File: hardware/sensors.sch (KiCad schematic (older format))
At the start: 43 parts, among them P13 CONN_01X02_MTMP, P14 CONN_01X02_BTMP, U1 LM358A, U2 LAH-100P, U3 LOC110, U4 MCP6001, U5 ADA4805-1

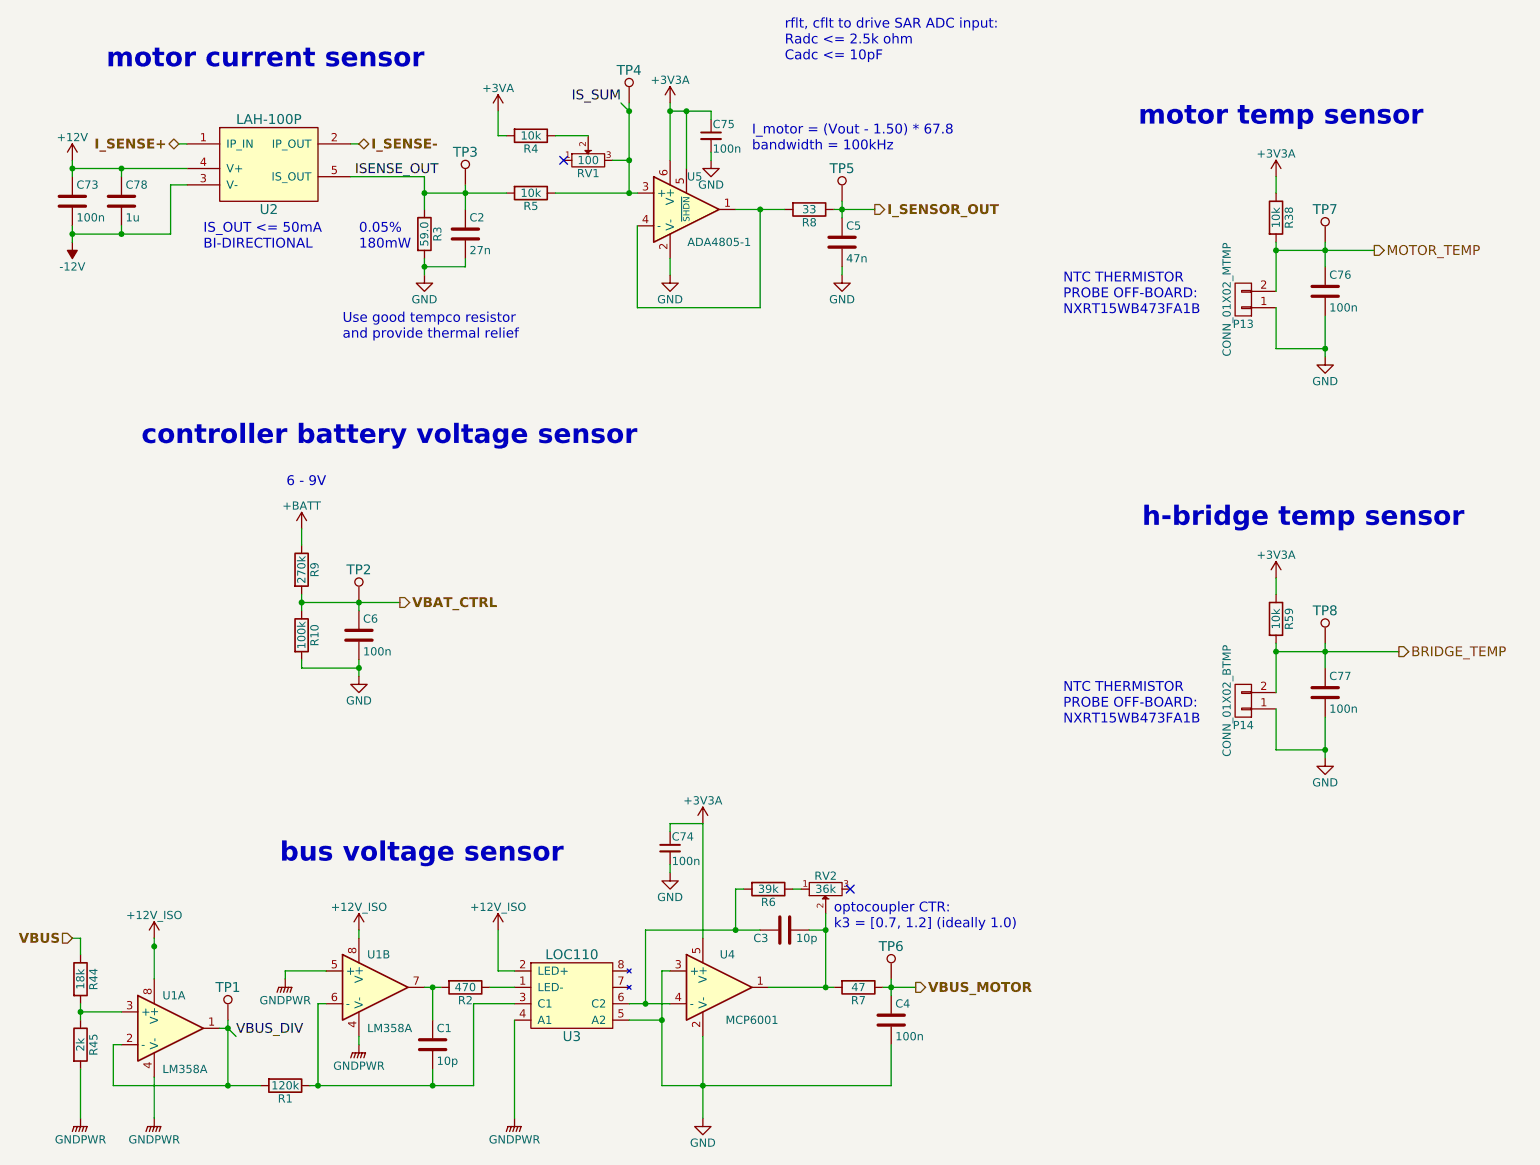
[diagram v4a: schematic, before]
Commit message: Create and verify full Digikey BOM
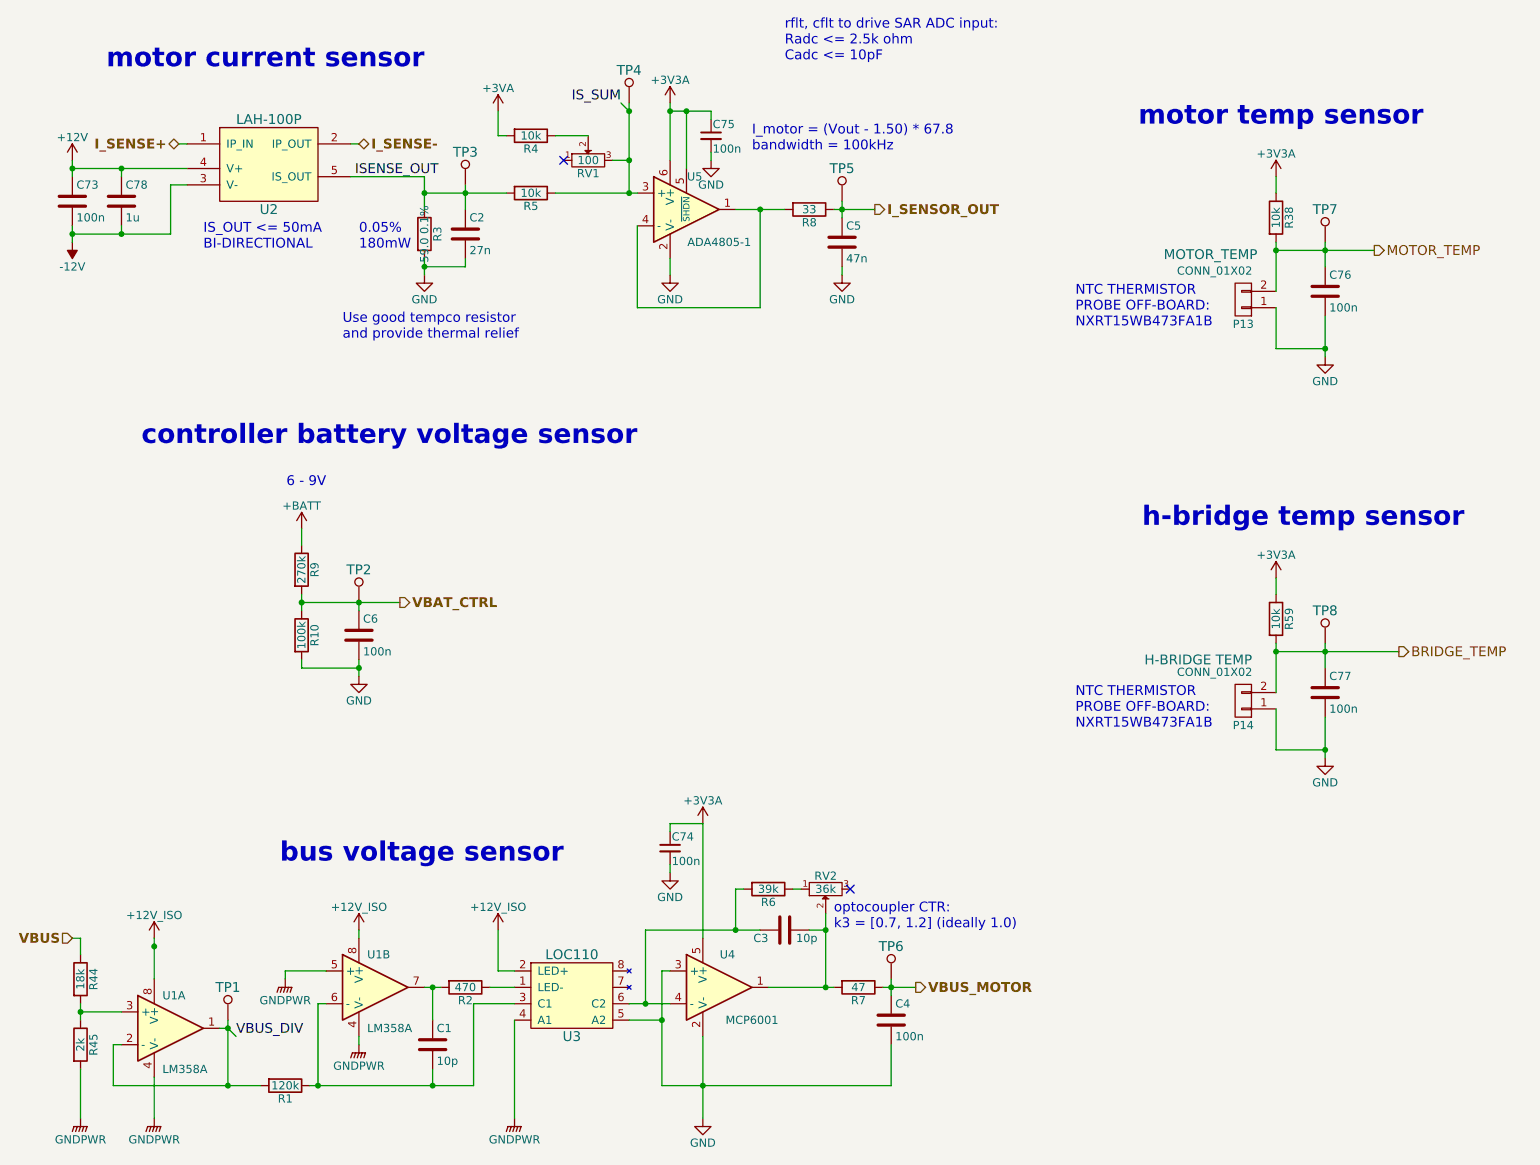
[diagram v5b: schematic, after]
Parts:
- C1, C2, C3, C4, C5, C6, C74, C75, C76, C77: Voltage (none) -> 16V
- C73, C78: Voltage (none) -> 25V
- P13: value CONN_01X02_MTMP -> CONN_01X02; Use (none) -> MOTOR_TEMP
- P14: value CONN_01X02_BTMP -> CONN_01X02; Use (none) -> H-BRIDGE TEMP
- R3: value 59.0 -> 59.0 0.1%
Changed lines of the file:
@@
 P 3100 2000
 F 0 "R3" V 3180 2000 50  0000 C CNN
-F 1 "59.0" V 3100 2000 50  0000 C CNN
+F 1 "59.0 0.1%" V 3100 2000 50  0000 C CNN
 F 2 "Resistors_SMD:R_1206" V 3030 2000 50  0001 C CNN
 F 3 "" H 3100 2000 50  0000 C CNN
@@
 F 2 "Capacitors_SMD:C_0603" H 3388 1850 50  0001 C CNN
 F 3 "" H 3350 2000 50  0000 C CNN
+F 4 "16V" H 3350 2000 60  0001 C CNN "Voltage"
 	1    3350 2000
 	1    0    0    -1
@@
 F 2 "Capacitors_SMD:C_0603" H 3188 6800 50  0001 C CNN
 F 3 "" H 3150 6950 50  0000 C CNN
+F 4 "16V" H 3150 6950 60  0001 C CNN "Voltage"
 	1    3150 6950
 	1    0    0    -1
@@
 F 2 "Capacitors_SMD:C_0603" H 5338 6100 50  0001 C CNN
 F 3 "" H 5300 6250 50  0000 C CNN
+F 4 "16V" V 5300 6250 60  0001 C CNN "Voltage"
 	1    5300 6250
 	0    -1   -1   0
@@
 F 2 "Capacitors_SMD:C_0603" H 5688 1900 50  0001 C CNN
 F 3 "" H 5650 2050 50  0000 C CNN
+F 4 "16V" H 5650 2050 60  0001 C CNN "Voltage"
 	1    5650 2050
 	1    0    0    -1
@@
 F 2 "Capacitors_SMD:C_0603" H 5988 6650 50  0001 C CNN
 F 3 "" H 5950 6800 50  0000 C CNN
+F 4 "16V" H 5950 6800 60  0001 C CNN "Voltage"
 	1    5950 6800
 	1    0    0    -1
@@
 F 2 "Capacitors_SMD:C_0603" H 8638 2200 50  0001 C CNN
 F 3 "" H 8600 2350 50  0000 C CNN
+F 4 "16V" H 8600 2350 60  0001 C CNN "Voltage"
 	1    8600 2350
 	1    0    0    -1
@@
 F 2 "Capacitors_SMD:C_0603" H 4850 1400 50  0001 C CNN
 F 3 "" H 4850 1400 50  0000 C CNN
+F 4 "16V" H 4850 1400 60  0001 C CNN "Voltage"
 	1    4850 1400
 	1    0    0    -1
@@
 F 2 "Capacitors_SMD:C_0603" H 4600 5750 50  0001 C CNN
 F 3 "" H 4600 5750 50  0000 C CNN
+F 4 "16V" H 4600 5750 60  0001 C CNN "Voltage"
 	1    4600 5750
 	1    0    0    -1
@@
 F 2 "Capacitors_SMD:C_0603" H 8638 4650 50  0001 C CNN
 F 3 "" H 8600 4800 50  0000 C CNN
+F 4 "16V" H 8600 4800 60  0001 C CNN "Voltage"
 	1    8600 4800
 	1    0    0    -1
@@
 F 2 "Capacitors_SMD:C_0603" H 2738 4300 50  0001 C CNN
 F 3 "" H 2700 4450 50  0000 C CNN
+F 4 "16V" H 2700 4450 60  0001 C CNN "Voltage"
 	1    2700 4450
 	1    0    0    -1
@@
 F 2 "Capacitors_SMD:C_0603" H 988 1650 50  0001 C CNN
 F 3 "" H 950 1800 50  0000 C CNN
+F 4 "25V" H 950 1800 60  0001 C CNN "Voltage"
 	1    950  1800
 	1    0    0    -1
@@
 F 2 "Capacitors_SMD:C_0603" H 1288 1650 50  0001 C CNN
 F 3 "" H 1250 1800 50  0000 C CNN
+F 4 "25V" H 1250 1800 60  0001 C CNN "Voltage"
 	1    1250 1800
 	1    0    0    -1
@@
 P 8100 2400
 F 0 "P13" H 8100 2550 50  0000 C CNN
-F 1 "CONN_01X02_MTMP" V 8200 2400 50  0000 C CNN
+F 1 "CONN_01X02" H 8275 2225 50  0000 C CNN
 F 2 "2kwMotorController:TERM_2P_2-5_1990009" H 8100 2400 50  0001 C CNN
 F 3 "" H 8100 2400 50  0000 C CNN
+F 4 "MOTOR_TEMP" H 8300 2125 60  0000 C CNN "Use"
 	1    8100 2400
 	-1   0    0    1
 $EndComp
-Text Notes 7000 2500 0    60   ~ 0
+Text Notes 7075 2575 0    60   ~ 0
 NTC THERMISTOR\nPROBE OFF-BOARD:\nNXRT15WB473FA1B
-Text Notes 7000 5000 0    60   ~ 0
+Text Notes 7075 5025 0    60   ~ 0
 NTC THERMISTOR\nPROBE OFF-BOARD:\nNXRT15WB473FA1B
 $Comp
@@
 P 8100 4850
 F 0 "P14" H 8100 5000 50  0000 C CNN
-F 1 "CONN_01X02_BTMP" V 8200 4850 50  0000 C CNN
+F 1 "CONN_01X02" H 8275 4675 50  0000 C CNN
 F 2 "2kwMotorController:TERM_2P_2-5_1990009" H 8100 4850 50  0001 C CNN
 F 3 "" H 8100 4850 50  0000 C CNN
+F 4 "H-BRIDGE TEMP" H 8375 4600 60  0000 C CNN "Use"
 	1    8100 4850
 	-1   0    0    1

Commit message: Open Loop Test Code
Rough version of control task for open loop testing of H-bridge
Rough version of sensor code
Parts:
- RV1, RV2: symbol POT -> POT-RESCUE-2kwMotorController
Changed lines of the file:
@@
 EESchema Schematic File Version 2
+LIBS:2kwMotorController-rescue
 LIBS:power
 LIBS:device
@@
 optocoupler CTR:\nk3 = [0.7, 1.2] (ideally 1.0)
 $Comp
-L POT RV2
+L POT-RESCUE-2kwMotorController RV2
 U 1 1 599D4CE6
 P 5550 6000
@@
 $EndComp
 $Comp
-L POT RV1
+L POT-RESCUE-2kwMotorController RV1
 U 1 1 59A7AA70
 P 4100 1550

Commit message: Revised layout mostly complete
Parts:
- P13, P14: footprint 2kwMotorController:TERM_2P_2-5_1990009 -> Pin_Headers:Pin_Header_Straight_1x02
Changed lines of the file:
@@
 F 0 "P13" H 8100 2550 50  0000 C CNN
 F 1 "CONN_01X02" H 8275 2225 50  0000 C CNN
-F 2 "2kwMotorController:TERM_2P_2-5_1990009" H 8100 2400 50  0001 C CNN
+F 2 "Pin_Headers:Pin_Header_Straight_1x02" H 8100 2400 50  0001 C CNN
 F 3 "" H 8100 2400 50  0000 C CNN
 F 4 "MOTOR_TEMP" H 8300 2125 60  0000 C CNN "Use"
@@
 F 0 "P14" H 8100 5000 50  0000 C CNN
 F 1 "CONN_01X02" H 8275 4675 50  0000 C CNN
-F 2 "2kwMotorController:TERM_2P_2-5_1990009" H 8100 4850 50  0001 C CNN
+F 2 "Pin_Headers:Pin_Header_Straight_1x02" H 8100 4850 50  0001 C CNN
 F 3 "" H 8100 4850 50  0000 C CNN
 F 4 "H-BRIDGE TEMP" H 8375 4600 60  0000 C CNN "Use"

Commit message: minor hw changes to submit PCB Rev 1
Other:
- note removed: "Use good tempco resistor\nand provide thermal relief"
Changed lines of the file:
@@
 Text HLabel 9050 4550 2    60   Output ~ 0
 BRIDGE_TEMP
-Text Notes 2600 2650 0    60   ~ 0
-Use good tempco resistor\nand provide thermal relief
 $Comp
 L R R8
